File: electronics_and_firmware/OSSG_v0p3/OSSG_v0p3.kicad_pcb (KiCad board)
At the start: 4 copper layers, 85 x 9 mm, 65 parts, among them IC1 DW01A, J1 USB_B_Micro, Q1 FS8205A, Q2 Q_NPN_BEC, Q3 Q_NPN_BEC, SW1 SW_SPST, U1 ESP32-PICO-D4, U2 TP4056, U3 XC6222B331MRG, U4 FT232RQ, U5 APX803L-29SA-7

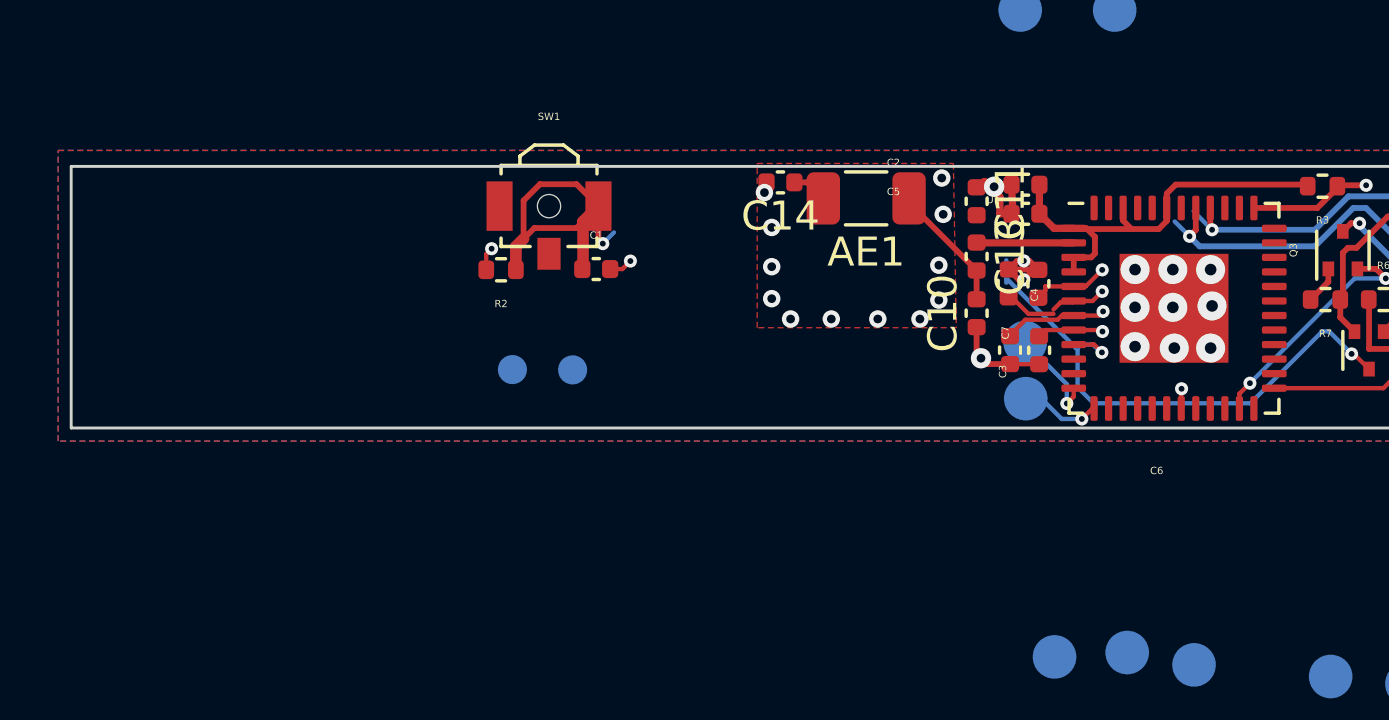
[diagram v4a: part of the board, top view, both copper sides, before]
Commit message: add microphone and external microphone breakout pads to left arm board schematic and layout
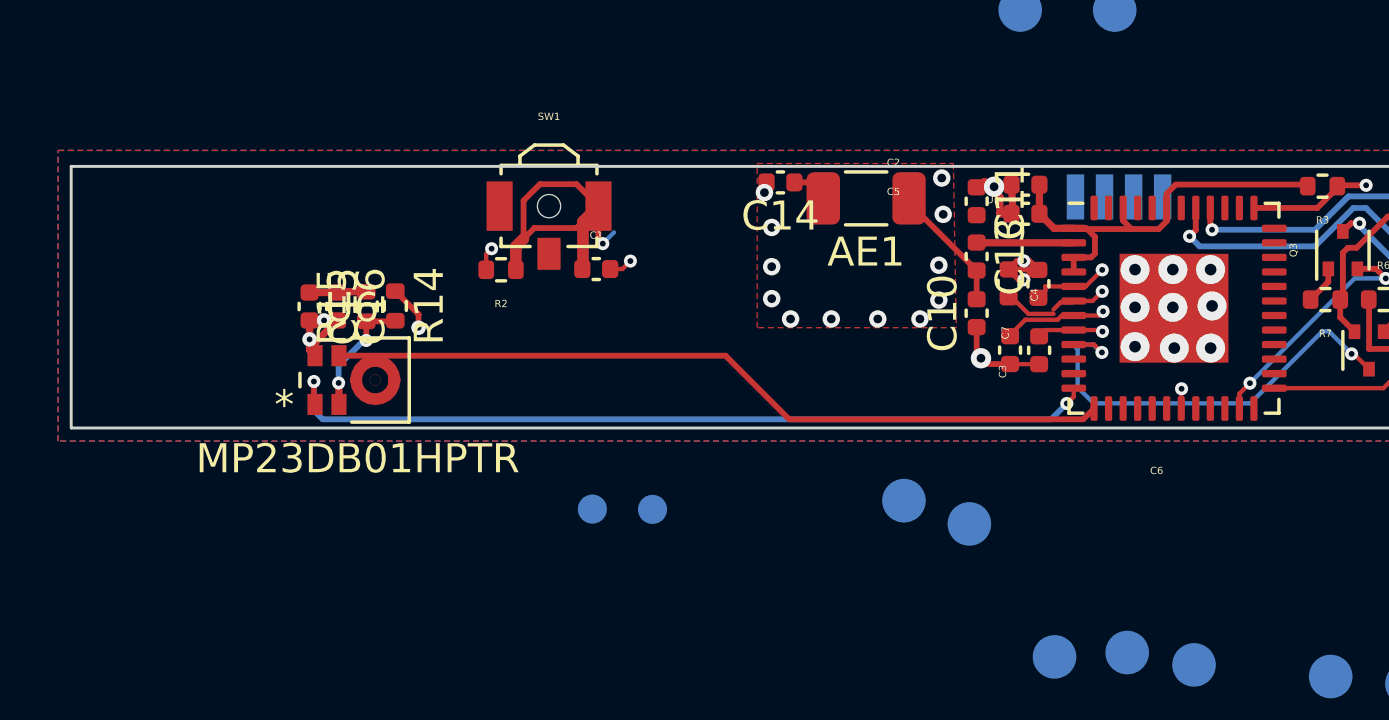
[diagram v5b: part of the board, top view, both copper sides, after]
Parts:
- added C15: 100nF/C0G, Capacitor_SMD:C_0402_1005Metric, F.Cu at (83.2, 79.8)
- added C16: 1uF/C0G, Capacitor_SMD:C_0402_1005Metric, F.Cu at (84.2, 79.8)
- added J2: External PDM Mic Input, footprints:Solder-4P-Connector, B.Cu at (111.0, 76.1)
- added R14: 10K*, Resistor_SMD:R_0402_1005Metric, F.Cu at (86.2, 79.8)
- added R15: 10K*, Resistor_SMD:R_0402_1005Metric, F.Cu at (85.2, 79.8)
- added U6: MP23DB01HPTR, footprints:MP23DB01HPTR, F.Cu at (84.8, 82.3)
- AE1: value Antenna_Chip -> H2U34W1H1Z0400
- moved TP22 6.53 mm to (105.9, 87.3)
- moved TP3 5.53 mm to (92.9, 86.8)
- moved TP4 5.53 mm to (95.0, 86.8)
- moved TP24 5.47 mm to (103.7, 86.5)
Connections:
- U1 pad 28: IO9 -> EXT1_MIC_DATA
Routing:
- net IO32: track 3.32 -> 28.7 mm, vias 1 -> 2
- net IO33: track 2.31 -> 27.1 mm, vias 1 -> 0
- net +3V3: track 17.1 -> 22.6 mm, vias 5 -> 8
- net Net-(R14-Pad2): track 0.00 -> 4.32 mm, vias 0 -> 2
- net EN: track 31.7 -> 27.5 mm
- net GND: track 47.9 -> 49.9 mm
- net RX_ESP: track 12.3 -> 11.4 mm
- net TX_ESP: track 11.7 -> 10.9 mm

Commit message: Layout and schematic tidying
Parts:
- C10, C11, C13: value C_Small -> NC
- C14: value C_Small -> Fine Tuning
- moved GND 38.7 mm to (125.1, 76.2)
- moved 3.3V 36.3 mm to (127.6, 76.2)
- moved RX 29.3 mm to (122.2, 76.0)
- moved TX 29.1 mm to (120.3, 77.0)
- moved IO32 18.3 mm to (88.1, 83.0)
- moved IO33 14.1 mm to (90.1, 82.6)
- moved TP10 13.4 mm to (109.3, 78.5)
- moved IO15 13.4 mm to (124.5, 82.9)
- moved IO2 12.3 mm to (124.5, 81.0)
- moved TP11 12.0 mm to (107.4, 78.0)
- moved BATT+ 11.9 mm to (156.7, 76.5)
- moved IO4 11.5 mm to (122.5, 83.0)
- moved BATT- 11.4 mm to (158.7, 76.5)
- moved IO14 11.0 mm to (108.2, 82.6)
- moved TP12 10.8 mm to (107.4, 79.8)
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- renumbered TP17 to 3.3V, TP14 to BATT+, TP16 to BATT-, TP18 to GND, TP21 to IO13, TP20 to IO14, TP19 to IO15, TP5 to IO2, TP6 to IO25, TP7 to IO26, TP22 to IO32, TP24 to IO33, TP1 to IO4, TP4 to RX, TP3 to TX
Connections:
- net IO8 renamed EXT1_MIC_CLK
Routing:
- net IO15: track 0.00 -> 14.6 mm, vias 0 -> 1
- net BATT+: track 16.4 -> 28.8 mm, vias 0 -> 2
- net IO2: track 0.00 -> 12.2 mm, vias 0 -> 1
- net EN: track 27.5 -> 39.5 mm, vias 3 -> 2
- net IO13: track 0.00 -> 9.64 mm, vias 0 -> 1
- net +3V3: track 22.6 -> 13.9 mm, vias 8 -> 10
- net IO25: track 0.00 -> 8.42 mm, vias 0 -> 1
- net IO4: track 0.00 -> 7.72 mm, vias 0 -> 1
- net EXT1_MIC_DATA: track 0.00 -> 7.54 mm, vias 0 -> 1
- net EXT1_MIC_CLK: track 0.00 -> 6.82 mm, vias 0 -> 1
- net IO26: track 0.00 -> 6.55 mm, vias 0 -> 1
- net IO14: track 0.00 -> 6.38 mm, vias 0 -> 1
- net ADC1C2: track 2.68 -> 6.96 mm
- net ADC1C1: track 3.58 -> 7.61 mm
- net ADC1C3: track 2.29 -> 5.80 mm, vias 1 -> 2
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
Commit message: Graphical fixes
Added silkscreen for adc testpoints
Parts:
- renumbered TP10 to ADC0, TP11 to ADC1, TP2 to ADC2, TP12 to ADC3
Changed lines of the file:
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@@
     (property "Sheetname" "")
     (attr smd)
-    (fp_text reference "TP2" (at 0.55 -1.6 unlocked) (layer "B.SilkS")
-      (effects (font (size 0.25 0.25) (thickness 0.025)) (justify mirror))
+    (fp_text reference "ADC2" (at 1.85 -1.25 unlocked) (layer "B.SilkS")
+      (effects (font (size 0.5 0.5) (thickness 0.025)) (justify mirror))
     )
     (fp_text value "IO36_ADC1C2" (at 0 -2.25 unlocked) (layer "B.Fab")
@@
     (property "Sheetname" "")
     (attr smd)
-    (fp_text reference "TP11" (at 0.05 2.4 unlocked) (layer "B.SilkS")
-      (effects (font (size 0.25 0.25) (thickness 0.025)) (justify mirror))
+    (fp_text reference "ADC1" (at 1.45 -0.9 unlocked) (layer "B.SilkS")
+      (effects (font (size 0.5 0.5) (thickness 0.025)) (justify mirror))
     )
     (fp_text value "IO38_ADC1C1" (at 0 -2.25 unlocked) (layer "B.Fab")
@@
     (property "Sheetname" "")
     (attr smd)
-    (fp_text reference "TP10" (at 0 2.25 unlocked) (layer "B.SilkS")
-      (effects (font (size 0.25 0.25) (thickness 0.025)) (justify mirror))
+    (fp_text reference "ADC0" (at 0 -1.25 unlocked) (layer "B.SilkS")
+      (effects (font (size 0.5 0.5) (thickness 0.025)) (justify mirror))
     )
     (fp_text value "IO37_ADC1C0" (at 0 -2.25 unlocked) (layer "B.Fab")
@@
     (property "Sheetname" "")
     (attr smd)
-    (fp_text reference "TP12" (at 0 2.25 unlocked) (layer "B.SilkS")
-      (effects (font (size 0.25 0.25) (thickness 0.025)) (justify mirror))
+    (fp_text reference "ADC3" (at -1.85 -0.7 unlocked) (layer "B.SilkS")
+      (effects (font (size 0.5 0.5) (thickness 0.025)) (justify mirror))
     )
     (fp_text value "IO39_ADC1C3" (at 0 -2.25 unlocked) (layer "B.Fab")
@@
       (net 33 "IO2") (pinfunction "1") (pintype "passive"))
   )
+  (gr_line (start 106.3 78.05) (end 106.05 78.05) (layer "B.SilkS") (width 0.15))
+  (gr_line (start 105.95 78.4) (end 106.15 78.2) (layer "B.SilkS") (width 0.15))
+  (gr_line (start 106.3 78.3) (end 106.3 78.05) (layer "B.SilkS") (width 0.15))
+  (gr_line (start 106.15 78.2) (end 106.3 78.05) (layer "B.SilkS") (width 0.15))
+  (gr_line (start 105.9 76.3) (end 106.2 76.3) (layer "B.SilkS") (width 0.15))
+  (gr_line (start 106.2 76.3) (end 106.2 76.6) (layer "B.SilkS") (width 0.15))
+  (gr_line (start 105.75 76.75) (end 106.2 76.3) (layer "B.SilkS") (width 0.15))
+  (gr_line (start 106.3 78.05) (end 106.3 78.3) (layer "B.SilkS") (width 0.15))
+  (gr_line (start 106.2 76.3) (end 105.9 76.3) (layer "B.SilkS") (width 0.15))
   (gr_line (start 75 84) (end 75 75) (layer "Edge.Cuts") (width 0.1))
   (gr_line (start 75 75) (end 160 75) (layer "Edge.Cuts") (width 0.1))

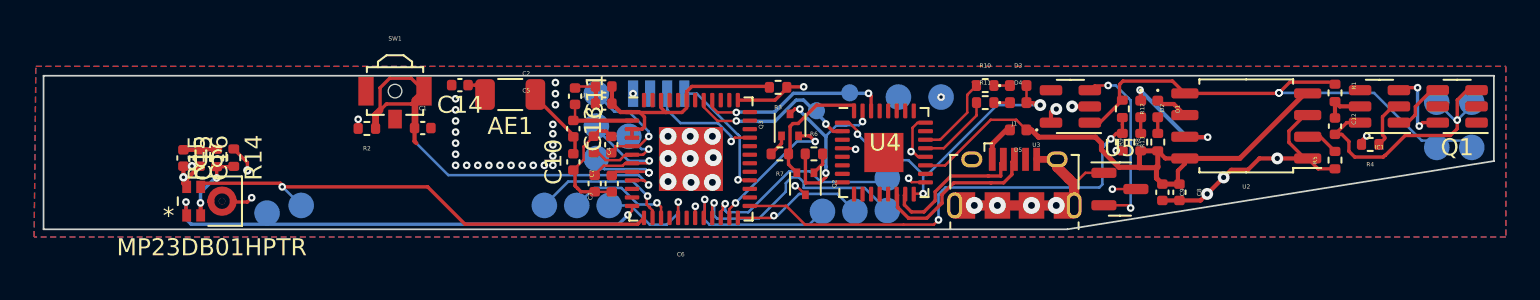
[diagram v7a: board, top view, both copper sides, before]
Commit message: add io0 and en TPs, fix silk screen, add missing capacitors, add ground pour and exposed pad for thermals under ESP32-PICO-D4
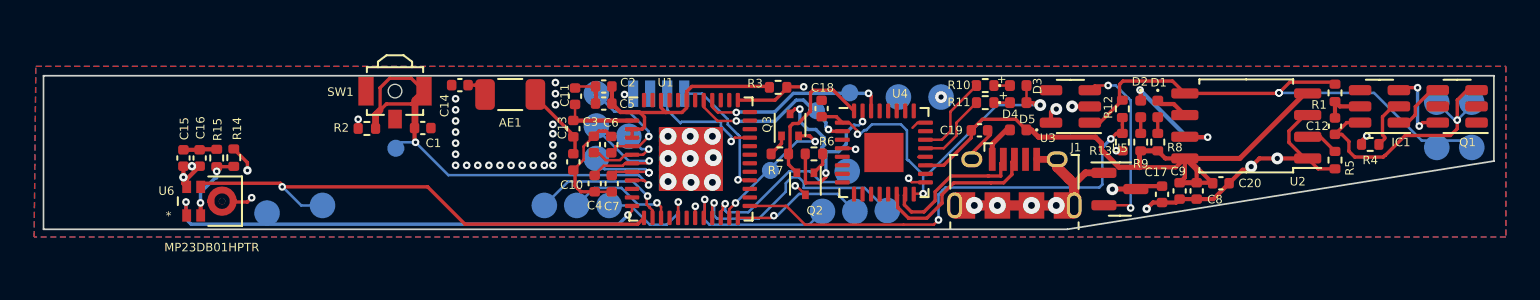
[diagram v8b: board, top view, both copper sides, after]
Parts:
- added C17: 0.1uF, Capacitor_SMD:C_0402_1005Metric, F.Cu at (140.6, 82.0)
- added C18: 0.1uF, Capacitor_SMD:C_0402_1005Metric, F.Cu at (120.6, 76.9)
- added C19: 0.1uF, Capacitor_SMD:C_0402_1005Metric, F.Cu at (129.8, 78.2)
- added C20: 0.1uF, Capacitor_SMD:C_0402_1005Metric, F.Cu at (144.0, 81.3)
- added TP8: EN_TP, TestPoint:TestPoint_Pad_D1.0mm, B.Cu at (95.7, 79.2)
- added TP9: IO0_TP, TestPoint:TestPoint_Pad_D1.0mm, B.Cu at (117.6, 80.5)
- moved TP5 2.38 mm to (122.1, 80.6)
- moved TP24 1.25 mm to (91.3, 82.6)
- moved C8 1.01 mm to (142.6, 81.8)
- moved C9 1.01 mm to (141.6, 81.8)
- renumbered IO4 to TP1, ADC0 to TP10, ADC1 to TP11, ADC3 to TP12, BATT+ to TP14, BATT- to TP16, 3.3V to TP17, GND to TP18, IO15 to TP19, ADC2 to TP2, IO14 to TP20, IO13 to TP21, IO32 to TP22, IO33 to TP24, TX to TP3, RX to TP4, IO2 to TP5, IO25 to TP6, IO26 to TP7
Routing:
- net VCC_IN: track 33.7 -> 38.4 mm
- net VCCIO: track 18.5 -> 21.3 mm
- net IO2: track 12.2 -> 10.0 mm
- net +3V3: track 13.9 -> 16.1 mm
- net GND: track 47.5 -> 49.0 mm, vias 46 -> 45
- net RTS: track 7.24 -> 8.72 mm
- net EN: track 39.5 -> 40.8 mm, vias 2 -> 3
- net IO33: track 28.9 -> 30.2 mm
- net DTR: track 11.7 -> 12.8 mm
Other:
- board text added: "+"
